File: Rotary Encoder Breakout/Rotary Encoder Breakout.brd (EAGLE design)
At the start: 17.8 x 25.4 mm, 2 parts, among them SW1 EC12E_SW

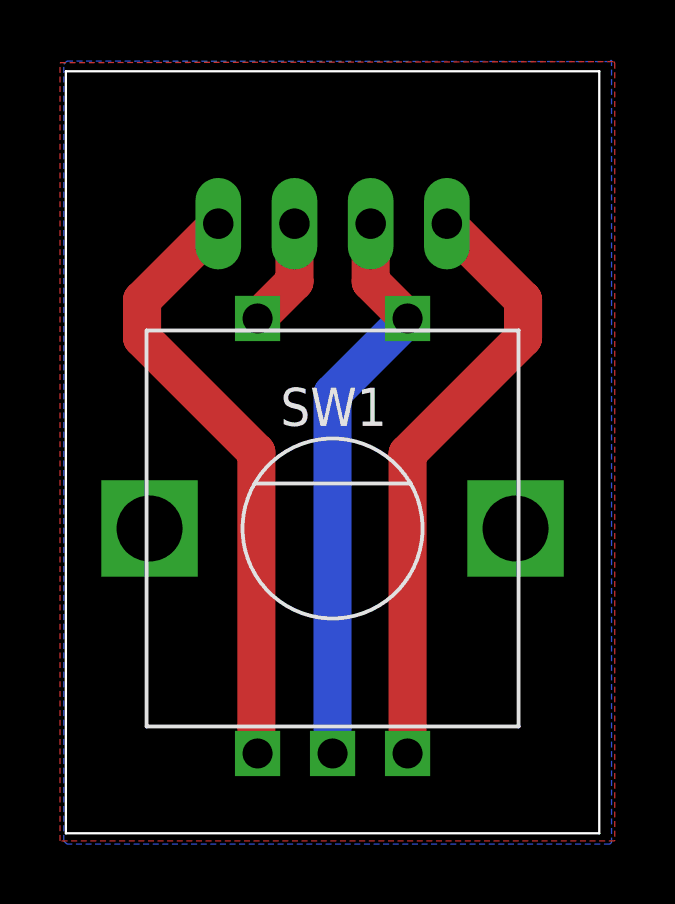
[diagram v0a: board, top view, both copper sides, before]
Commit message: Rename, add GND to mounting ears
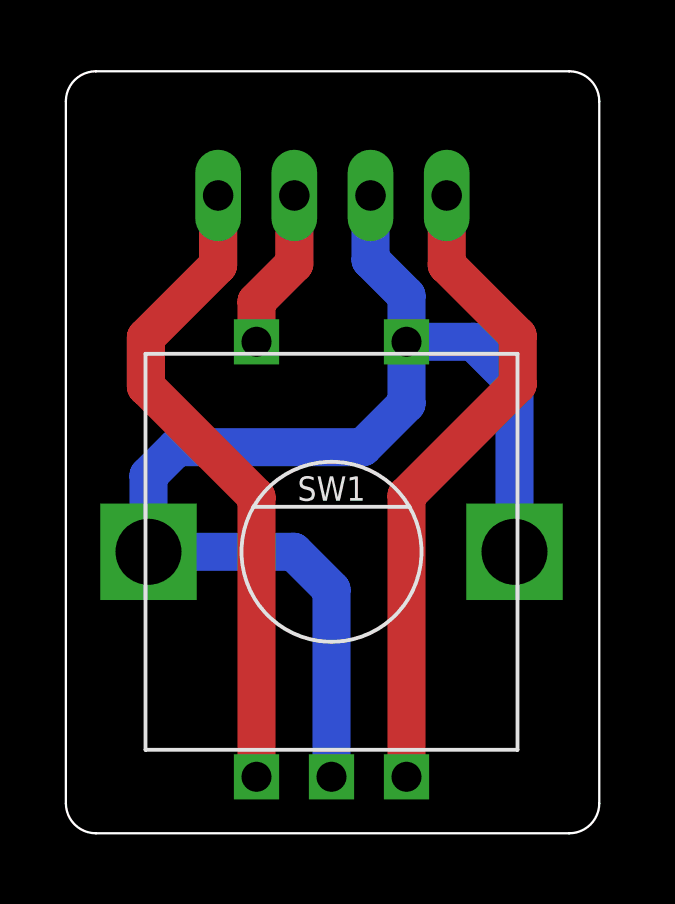
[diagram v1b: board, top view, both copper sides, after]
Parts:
- removed SV1: 4-Pin Header, LBussy:HEADER04-1
- added P1: HDR-4, Donnie:HDR-4_VERT
- SW1: value EC12E_SW -> SWITCH-ALPS_EC12E_SW; device switch-alps:ALPS_EC12E_SW -> Donnie:SWITCH-ALPS_ALPS_EC12E_SW
- moved SW1 0.78 mm to (8.85, 84.3)
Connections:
- net GND: now also P1.2, SW1.1, SW1.2; no longer SV1.3
- net PB: now also P1.3; no longer SV1.2
- net ROTA: now also P1.4, SW1.A; no longer SV1.4, SW1.B
- net ROTB: now also P1.1, SW1.B; no longer SV1.1, SW1.A
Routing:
- net GND: track 19.2 -> 42.2 mm
- net PB: track 3.67 -> 5.40 mm
- net ROTA: track 20.3 -> 21.9 mm
- net ROTB: track 20.3 -> 21.9 mm
- removed copper zone on layer 1, net GND
- removed copper zone on layer 16, net GND
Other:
- outline, holes or cut-outs redrawn
- board text added: "PB"
- board text removed: "PSH"
